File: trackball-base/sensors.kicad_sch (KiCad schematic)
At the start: 20 parts, among them U301 PMW3360DM-T2QU, U302 PMW3360DM-T2QU

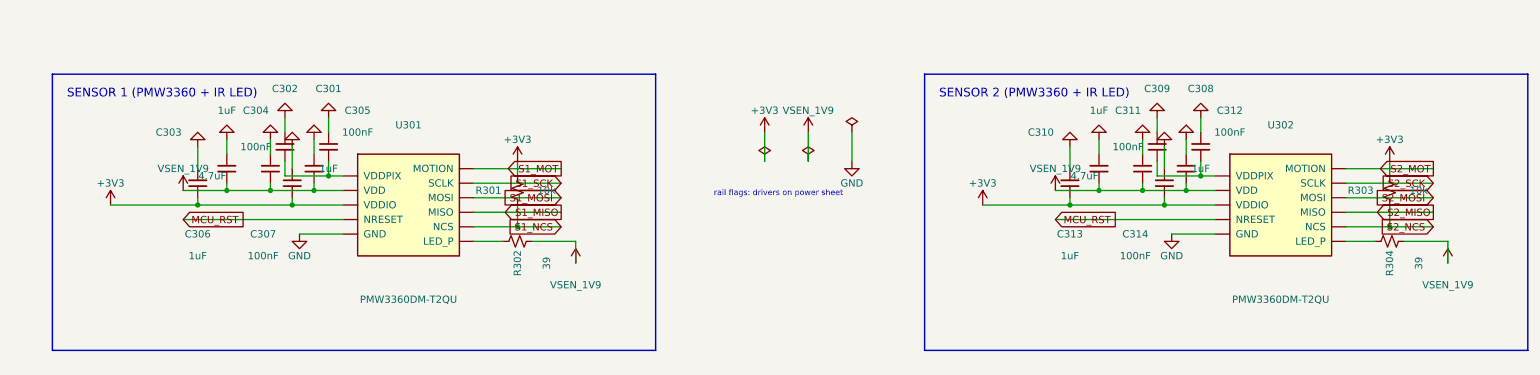
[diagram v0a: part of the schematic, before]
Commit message: base schematic complete: root + 5 sheets ERC-clean, review notes + BOM draft
Full hierarchical project (root + power/mcu/sensors/buttons/tx):
0 ERC errors, 1 benign pin_to_pin warning (ADC rail-sense, documented).
Netlist-verified: 145 comps, VSEN_1V9/MCU_RST/USB/SPI/TX nets.
Adds notes/SCHEMATIC_REVIEW.md (decisions, rail design, TX tree,
antenna, GPIO map, provisionals, ERC log) + notes/BOM_DRAFT.md.
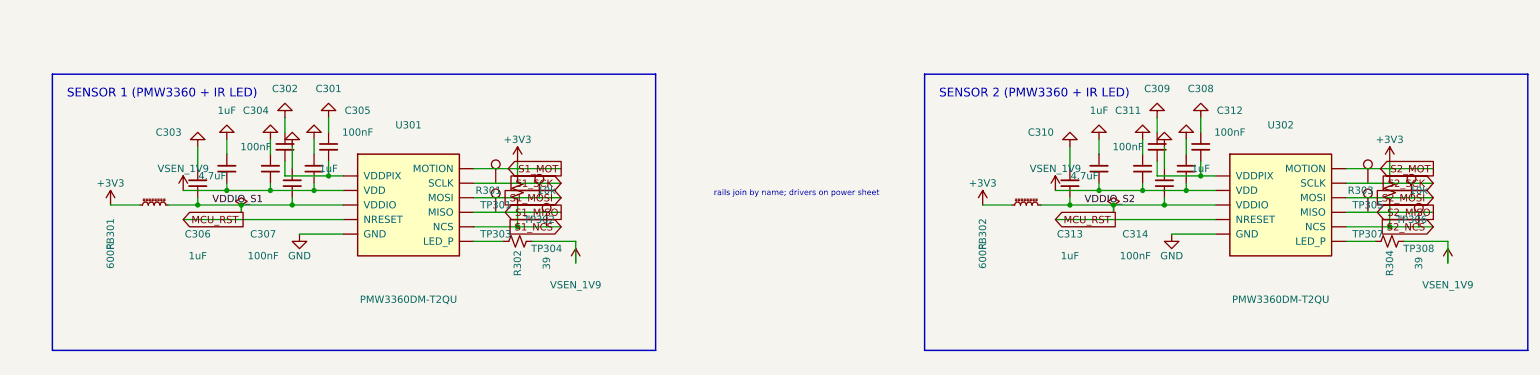
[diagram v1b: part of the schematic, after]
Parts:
- added FB301, FB302: 600R, Inductor_SMD:L_0603_1608Metric, symbol Device:L_Ferrite_Small
- added TP301: TP301, TestPoint:TestPoint_Pad_D1.5mm, symbol Connector:TestPoint
- added TP302: TP302, TestPoint:TestPoint_Pad_D1.5mm, symbol Connector:TestPoint
- added TP303: TP303, TestPoint:TestPoint_Pad_D1.5mm, symbol Connector:TestPoint
- added TP304: TP304, TestPoint:TestPoint_Pad_D1.5mm, symbol Connector:TestPoint
- added TP305: TP305, TestPoint:TestPoint_Pad_D1.5mm, symbol Connector:TestPoint
- added TP306: TP306, TestPoint:TestPoint_Pad_D1.5mm, symbol Connector:TestPoint
- added TP307: TP307, TestPoint:TestPoint_Pad_D1.5mm, symbol Connector:TestPoint
- added TP308: TP308, TestPoint:TestPoint_Pad_D1.5mm, symbol Connector:TestPoint
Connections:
- net +3V3: now also FB301.1, FB302.1; no longer C306.2, C307.2, C313.2, C314.2, U301.5 (VDDIO), U302.5 (VDDIO)
- net S1_MISO: now also TP303.1
- net S1_MOSI: now also TP302.1
- net S1_NCS: now also TP304.1
- net S1_SCK: now also TP301.1
- net S2_MISO: now also TP307.1
- net S2_MOSI: now also TP306.1
- net S2_NCS: now also TP308.1
- net S2_SCK: now also TP305.1
- new net VDDIO_S1: C306.2, C307.2, FB301.2, U301.5 (VDDIO)
- new net VDDIO_S2: C313.2, C314.2, FB302.2, U302.5 (VDDIO)
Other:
- note added: "rails join by name; drivers on power sheet"
- note removed: "rail flags: drivers on power sheet"

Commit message: layout: placed+silk+parity-0 (drc10: 0 errors/0 parity, 125 warnings)
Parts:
- U301, U302: footprint (none) -> trackball:PMW3360DM-T2QU
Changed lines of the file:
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@@
         ))
     )
-    (property "Footprint" ""
+    (property "Description" "PixArt PMW3360DM-T2QU gaming sensor"
+    	(id 4)
+    	(at 0 0 0)
+    	(effects (font (size 1.27 1.27)) hide)
+    )
+    (property "Footprint" "trackball:PMW3360DM-T2QU"
       (at 128.27 152.40 0)
       (effects (font (size 1.27 1.27)) hide)
     )
-    (property "Datasheet" ""
+    (property "Datasheet" "PMW3360 datasheet v1.50"
       (at 128.27 152.40 0)
       (effects (font (size 1.27 1.27)) hide)
@@
         ))
     )
-    (property "Footprint" ""
+    (property "Description" "PixArt PMW3360DM-T2QU gaming sensor"
+    	(id 4)
+    	(at 0 0 0)
+    	(effects (font (size 1.27 1.27)) hide)
+    )
+    (property "Footprint" "trackball:PMW3360DM-T2QU"
       (at 280.67 152.40 0)
       (effects (font (size 1.27 1.27)) hide)
     )
-    (property "Datasheet" ""
+    (property "Datasheet" "PMW3360 datasheet v1.50"
       (at 280.67 152.40 0)
       (effects (font (size 1.27 1.27)) hide)

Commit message: WIP routing drc143: unc 57, 0 viol, VBUS12/GND11
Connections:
- net Net-(U302-VDDPIX): now reaches C308.2, C309.2, U302.3 (VDDPIX)
- net Net-(U301-VDDPIX): now reaches C301.2, C302.2, U301.3 (VDDPIX)
- net Net-(U302-LED_P): now reaches R304.1, U302.15 (LED_P)
- net Net-(U301-LED_P): now reaches R302.1, U301.15 (LED_P)
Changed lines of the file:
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@@
     (color 0 0 0 0)
   )
+  (label "Net-(U301-LED_P)"
+    (at 144.78 158.75 0)
+    (effects
+        (font
+          (size 1.27 1.27)
+        )
+        (justify left bottom))
+  )
+  (label "Net-(U301-VDDPIX)"
+    (at 114.30 144.78 90)
+    (effects
+        (font
+          (size 1.27 1.27)
+        )
+        (justify left bottom))
+  )
+  (label "Net-(U302-LED_P)"
+    (at 297.18 158.75 0)
+    (effects
+        (font
+          (size 1.27 1.27)
+        )
+        (justify left bottom))
+  )
+  (label "Net-(U302-VDDPIX)"
+    (at 266.70 144.78 90)
+    (effects
+        (font
+          (size 1.27 1.27)
+        )
+        (justify left bottom))
+  )
 )
